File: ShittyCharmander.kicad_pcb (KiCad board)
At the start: 2 copper layers, 77.9 x 88.8 mm, 21 parts, among them J1 Conn_02x02_Odd_Even, J2 Conn_02x03_Counter_Clockwise, U1 TPS60151, U2 ATTINY85-20MU

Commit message: Moved back silkscreen text to not intersect with vias
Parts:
- moved REF*** 0.80 mm to (130.2, 104.5)
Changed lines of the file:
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@@
   )
   (module Symbols:OSHW-Logo_11.4x12mm_SilkScreen (layer B.Cu)
-    (at 129.921 103.759 180)
+    (at 130.175 104.521 180)
     (descr "Open Source Hardware Logo")
     (tags "Logo OSHW")
@@
     (effects (font (size 1.5 1.5) (thickness 0.3)) (justify mirror))
   )
-  (gr_text "Shitty Charmander v1" (at 131.064 113.538) (layer B.SilkS)
+  (gr_text "Shitty Charmander v1" (at 131.064 112.776) (layer B.SilkS)
     (effects (font (size 1.5 1.5) (thickness 0.3)) (justify mirror))
   )
-  (gr_text "Inspired by \nAND!XOR" (at 130.302 117.602) (layer B.SilkS)
+  (gr_text "Inspired by \nAND!XOR" (at 129.794 118.618) (layer B.SilkS)
     (effects (font (size 1.5 1.5) (thickness 0.3)) (justify mirror))
   )

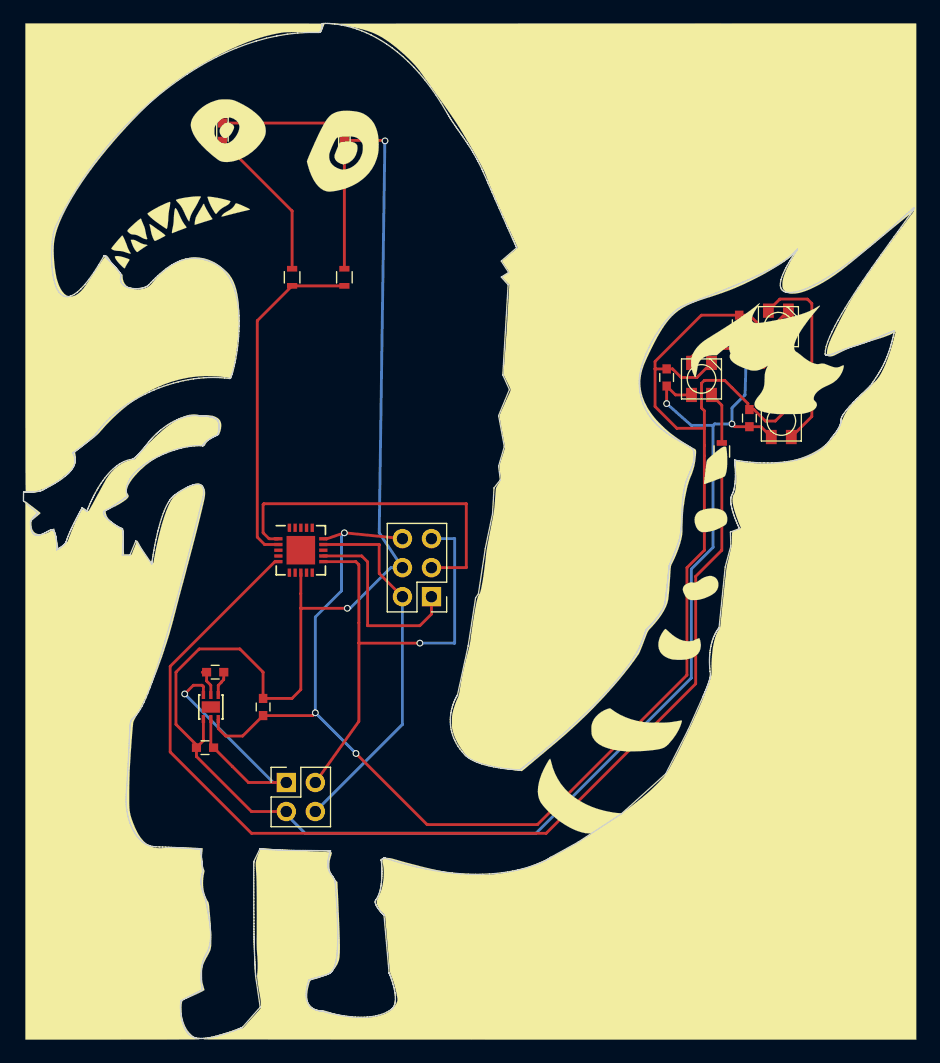
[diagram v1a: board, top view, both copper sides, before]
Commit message: Added clearance for arms for milling. Added gitignore
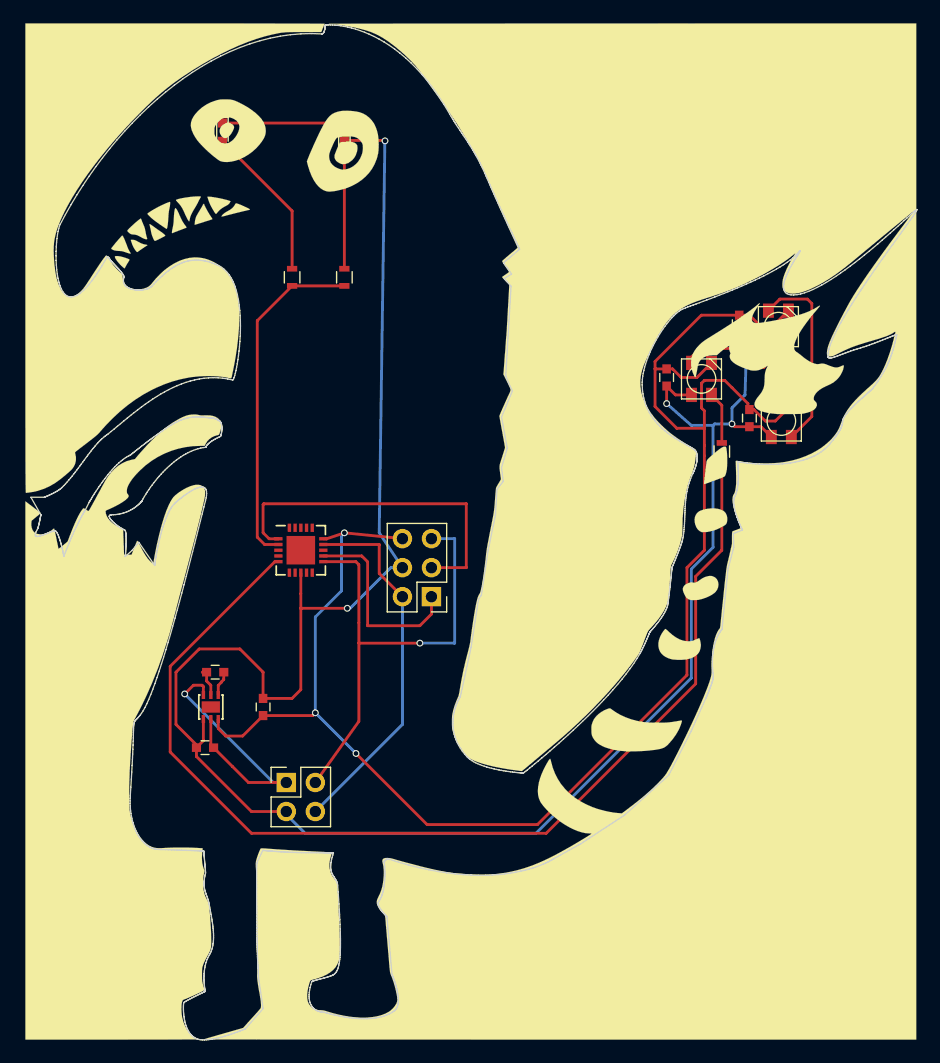
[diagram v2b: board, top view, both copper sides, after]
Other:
- board size 77.9 x 88.8 mm -> 77.5 x 88.8 mm

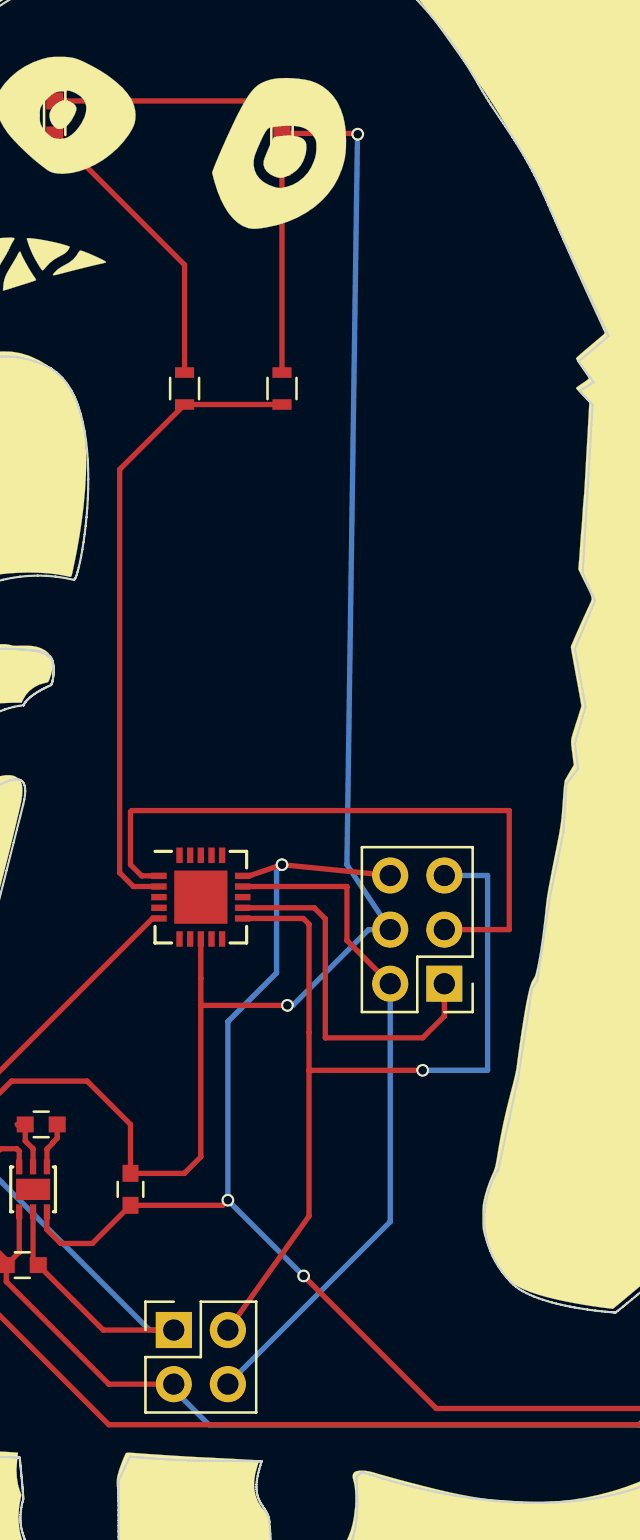
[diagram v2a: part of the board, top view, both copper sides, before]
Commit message: Fixed ISP header footprint and corrected the traces to match the correct pinout
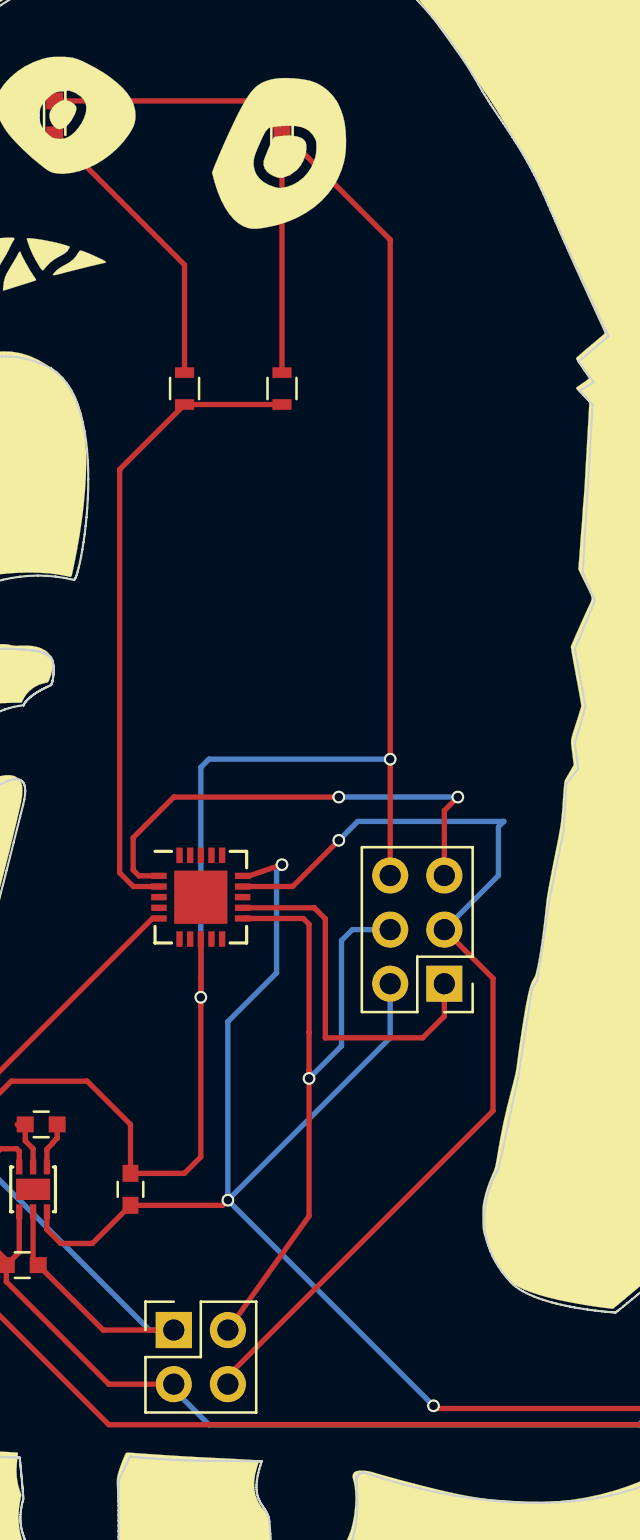
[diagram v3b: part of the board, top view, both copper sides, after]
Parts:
- J2: value Conn_02x03_Counter_Clockwise -> Conn_02x03_Odd_Even
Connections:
- J2 pad 2: SCK_SCL -> 5V
- J2 pad 3: RESET -> SCK_SCL
- J2 pad 4: GND -> MOSI_SDA
- J2 pad 5: MOSI_SDA -> RESET
- J2 pad 6: 5V -> GND
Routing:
- net SCK_SCL: track 32.2 -> 47.2 mm, vias 0 -> 1
- net MOSI_SDA: track 43.1 -> 33.1 mm
- net 5V: track 142.2 -> 150.4 mm
- net RESET: track 30.8 -> 23.1 mm, vias 0 -> 2
- net GND: track 200.4 -> 205.7 mm
